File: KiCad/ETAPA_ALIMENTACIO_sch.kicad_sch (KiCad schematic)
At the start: 14 parts, among them U4 LM2596S-5, U6 LM1117DT-3.3

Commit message: V1 Routing
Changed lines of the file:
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@@
+	)
+	(junction
+		(at 170.18 85.09)
+		(diameter 0)
+		(color 0 0 0 0)
 	)
 	(junction
@@
 	)
 	(junction
-		(at 160.02 85.09)
-		(diameter 0)
-		(color 0 0 0 0)
-	)
-	(junction
 		(at 199.39 104.14)
 		(diameter 0)
@@
 	(wire
 		(pts
-			(xy 160.02 85.09) (xy 166.37 85.09)
+			(xy 138.43 85.09) (xy 166.37 85.09)
 		)
 		(stroke
@@
 		(pts
 			(xy 182.88 104.14) (xy 187.96 104.14)
-		)
-		(stroke
-			(width 0)
-			(type default)
-		)
-	)
-	(wire
-		(pts
-			(xy 138.43 85.09) (xy 160.02 85.09)
 		)
 		(stroke
@@
 		(dnp no)
 		(fields_autoplaced yes)
-		(property "Reference" "#FLG07"
+		(property "Reference" "#FLG04"
 			(at 63.5 86.995 0)
 			(effects
@@
 			(project "PROJECTE_EINES"
 				(path "/347831db-5db9-4aff-ad32-e56fd770e219/b8d025f8-884e-44af-b29b-4fb2140b95b4"
-					(reference "#FLG07")
+					(reference "#FLG04")
 					(unit 1)
 				)
@@
 		(dnp no)
 		(fields_autoplaced yes)
-		(property "Reference" "#PWR050"
+		(property "Reference" "#PWR031"
 			(at 60.96 88.9 0)
 			(effects
@@
 			(project "PROJECTE_EINES"
 				(path "/347831db-5db9-4aff-ad32-e56fd770e219/b8d025f8-884e-44af-b29b-4fb2140b95b4"
-					(reference "#PWR050")
+					(reference "#PWR031")
 					(unit 1)
 				)
@@
 	)
 	(symbol
+		(lib_id "power:+5V")
+		(at 170.18 85.09 0)
+		(unit 1)
+		(exclude_from_sim no)
+		(in_bom yes)
+		(on_board yes)
+		(dnp no)
+		(fields_autoplaced yes)
+		(property "Reference" "#PWR049"
+			(at 170.18 88.9 0)
+			(effects
+				(font
+					(size 1.27 1.27)
+				)
+				(hide yes)
+			)
+		)
+		(property "Value" "+5V"
+			(at 170.18 80.01 0)
+			(effects
+				(font
+					(size 1.27 1.27)
+				)
+			)
+		)
+		(property "Footprint" ""
+			(at 170.18 85.09 0)
+			(effects
+				(font
+					(size 1.27 1.27)
+				)
+				(hide yes)
+			)
+		)
+		(property "Datasheet" ""
+			(at 170.18 85.09 0)
+			(effects
+				(font
+					(size 1.27 1.27)
+				)
+				(hide yes)
+			)
+		)
+		(property "Description" "Power symbol creates a global label with name \"+5V\""
+			(at 170.18 85.09 0)
+			(effects
+				(font
+					(size 1.27 1.27)
+				)
+				(hide yes)
+			)
+		)
+		(pin "1"
+		)
+		(instances
+			(project ""
+				(path "/347831db-5db9-4aff-ad32-e56fd770e219/b8d025f8-884e-44af-b29b-4fb2140b95b4"
+					(reference "#PWR049")
+					(unit 1)
+				)
+			)
+		)
+	)
+	(symbol
 		(lib_id "Device:C")
 		(at 97.79 88.9 0)
@@
 		(dnp no)
 		(fields_autoplaced yes)
-		(property "Reference" "#PWR040"
+		(property "Reference" "#PWR041"
 			(at 182.88 111.76 0)
 			(effects
@@
 			(project "PROJECTE_EINES"
 				(path "/347831db-5db9-4aff-ad32-e56fd770e219/b8d025f8-884e-44af-b29b-4fb2140b95b4"
-					(reference "#PWR040")
+					(reference "#PWR041")
 					(unit 1)
 				)
@@
 					(unit 1)
 				)
-			)
-		)
-	)
-	(symbol
-		(lib_id "power:+5V")
-		(at 160.02 85.09 0)
-		(unit 1)
-		(exclude_from_sim no)
-		(in_bom yes)
-		(on_board yes)
-		(dnp no)
-		(fields_autoplaced yes)
-		(property "Reference" "#PWR037"
-			(at 160.02 88.9 0)
-			(effects
-				(font
-					(size 1.27 1.27)
-				)
-				(hide yes)
-			)
-		)
-		(property "Value" "+5V"
-			(at 160.02 80.01 0)
-			(effects
-				(font
-					(size 1.27 1.27)
-				)
-			)
-		)
-		(property "Footprint" ""
-			(at 160.02 85.09 0)
-			(effects
-				(font
-					(size 1.27 1.27)
-				)
-				(hide yes)
-			)
-		)
-		(property "Datasheet" ""
-			(at 160.02 85.09 0)
-			(effects
-				(font
-					(size 1.27 1.27)
-				)
-				(hide yes)
-			)
-		)
-		(property "Description" "Power symbol creates a global label with name \"+5V\""
-			(at 160.02 85.09 0)
-			(effects
-				(font
-					(size 1.27 1.27)
-				)
-				(hide yes)
-			)
-		)
-		(pin "1"
-		)
-		(instances
-			(project "PROJECTE_EINES"
-				(path "/347831db-5db9-4aff-ad32-e56fd770e219/b8d025f8-884e-44af-b29b-4fb2140b95b4"
-					(reference "#PWR037")
-					(unit 1)
-				)

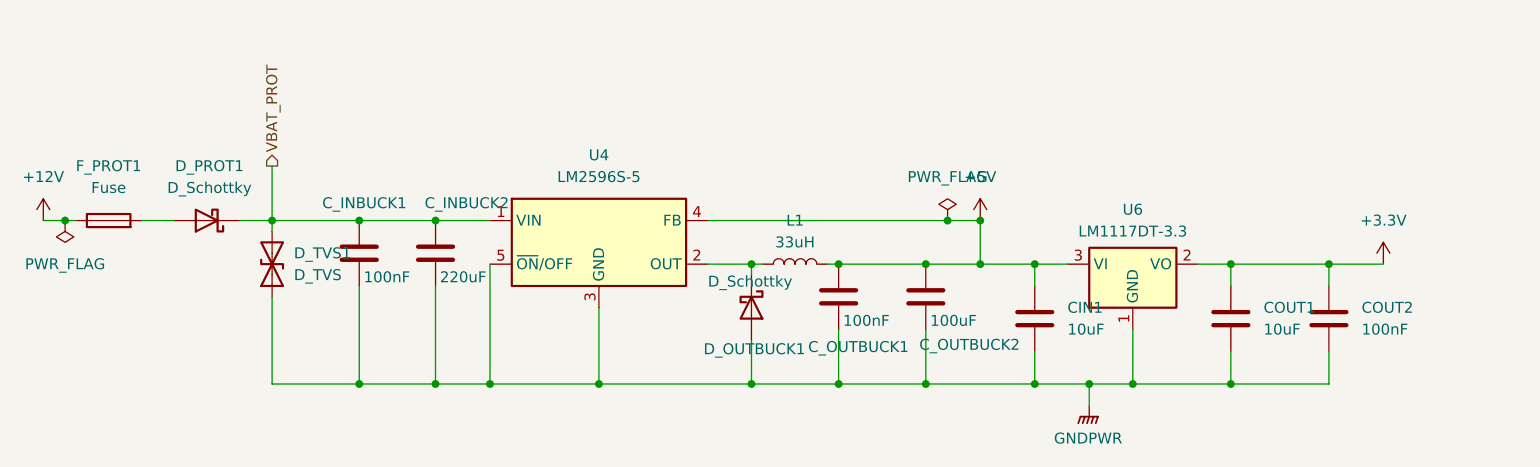
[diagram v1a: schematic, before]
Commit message: Actualització dels test points
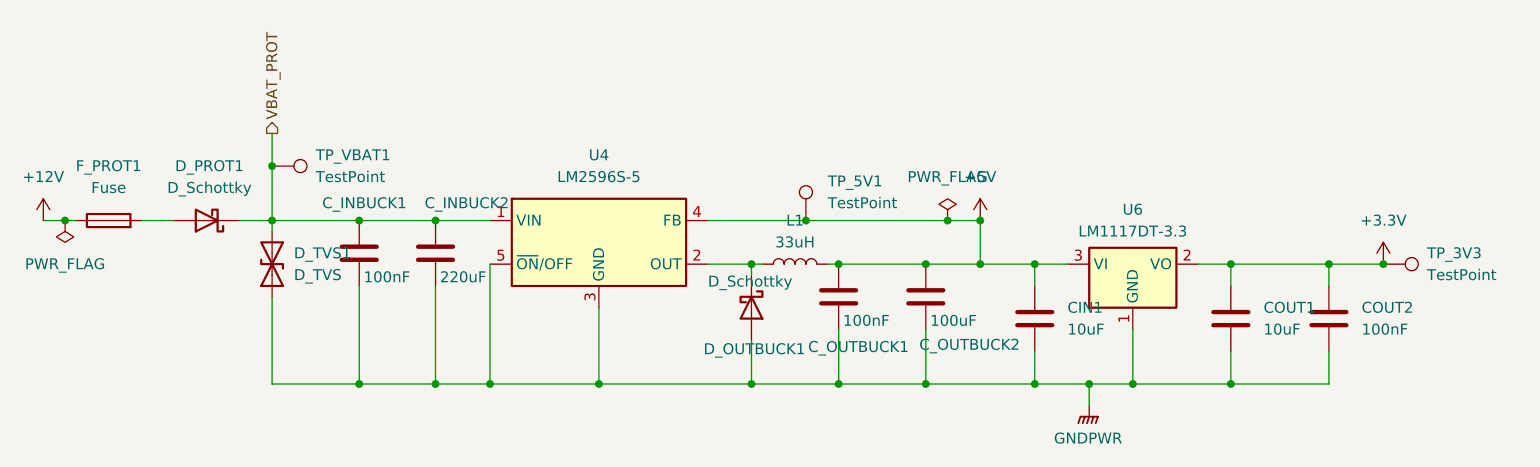
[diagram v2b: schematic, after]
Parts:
- added TP_3V3, TP_5V1, TP_VBAT1: TestPoint, TestPoint:TestPoint_Pad_D1.5mm, symbol Connector:TestPoint
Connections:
- net +3.3V: now also TP_3V3.1
- net +5V: now also TP_5V1.1
- net VBAT_PROT: now also TP_VBAT1.1
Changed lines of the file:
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@@
 	(paper "A4")
 	(junction
+		(at 217.17 90.17)
+		(diameter 0)
+		(color 0 0 0 0)
+	)
+	(junction
 		(at 97.79 85.09)
 		(diameter 0)
@@
 	)
 	(junction
+		(at 87.63 78.74)
+		(diameter 0)
+		(color 0 0 0 0)
+	)
+	(junction
 		(at 106.68 85.09)
 		(diameter 0)
@@
 	)
 	(junction
+		(at 149.86 85.09)
+		(diameter 0)
+		(color 0 0 0 0)
+	)
+	(junction
 		(at 166.37 85.09)
 		(diameter 0)
@@
 	(wire
 		(pts
+			(xy 149.86 85.09) (xy 166.37 85.09)
+		)
+		(stroke
+			(width 0)
+			(type default)
+		)
+	)
+	(wire
+		(pts
 			(xy 125.73 95.25) (xy 125.73 104.14)
 		)
@@
 	(wire
 		(pts
-			(xy 138.43 85.09) (xy 166.37 85.09)
+			(xy 138.43 85.09) (xy 149.86 85.09)
 		)
 		(stroke
@@
 	(wire
 		(pts
+			(xy 87.63 74.93) (xy 87.63 78.74)
+		)
+		(stroke
+			(width 0)
+			(type default)
+		)
+	)
+	(wire
+		(pts
+			(xy 106.68 85.09) (xy 113.03 85.09)
+		)
+		(stroke
+			(width 0)
+			(type default)
+		)
+	)
+	(wire
+		(pts
+			(xy 176.53 90.17) (xy 176.53 92.71)
+		)
+		(stroke
+			(width 0)
+			(type default)
+		)
+	)
+	(wire
+		(pts
+			(xy 87.63 85.09) (xy 97.79 85.09)
+		)
+		(stroke
+			(width 0)
+			(type default)
+		)
+	)
+	(wire
+		(pts
+			(xy 187.96 97.79) (xy 187.96 104.14)
+		)
+		(stroke
+			(width 0)
+			(type default)
+		)
+	)
+	(wire
+		(pts
+			(xy 106.68 92.71) (xy 106.68 104.14)
+		)
+		(stroke
+			(width 0)
+			(type default)
+		)
+	)
+	(wire
+		(pts
+			(xy 97.79 104.14) (xy 106.68 104.14)
+		)
+		(stroke
+			(width 0)
+			(type default)
+		)
+	)
+	(wire
+		(pts
+			(xy 199.39 100.33) (xy 199.39 104.14)
+		)
+		(stroke
+			(width 0)
+			(type default)
+		)
+	)
+	(wire
+		(pts
+			(xy 97.79 85.09) (xy 106.68 85.09)
+		)
+		(stroke
+			(width 0)
+			(type default)
+		)
+	)
+	(wire
+		(pts
+			(xy 182.88 104.14) (xy 187.96 104.14)
+		)
+		(stroke
+			(width 0)
+			(type default)
+		)
+	)
+	(wire
+		(pts
 			(xy 87.63 78.74) (xy 87.63 85.09)
-		)
-		(stroke
-			(width 0)
-			(type default)
-		)
-	)
-	(wire
-		(pts
-			(xy 106.68 85.09) (xy 113.03 85.09)
-		)
-		(stroke
-			(width 0)
-			(type default)
-		)
-	)
-	(wire
-		(pts
-			(xy 176.53 90.17) (xy 176.53 92.71)
-		)
-		(stroke
-			(width 0)
-			(type default)
-		)
-	)
-	(wire
-		(pts
-			(xy 87.63 85.09) (xy 97.79 85.09)
-		)
-		(stroke
-			(width 0)
-			(type default)
-		)
-	)
-	(wire
-		(pts
-			(xy 187.96 97.79) (xy 187.96 104.14)
-		)
-		(stroke
-			(width 0)
-			(type default)
-		)
-	)
-	(wire
-		(pts
-			(xy 106.68 92.71) (xy 106.68 104.14)
-		)
-		(stroke
-			(width 0)
-			(type default)
-		)
-	)
-	(wire
-		(pts
-			(xy 97.79 104.14) (xy 106.68 104.14)
-		)
-		(stroke
-			(width 0)
-			(type default)
-		)
-	)
-	(wire
-		(pts
-			(xy 199.39 100.33) (xy 199.39 104.14)
-		)
-		(stroke
-			(width 0)
-			(type default)
-		)
-	)
-	(wire
-		(pts
-			(xy 97.79 85.09) (xy 106.68 85.09)
-		)
-		(stroke
-			(width 0)
-			(type default)
-		)
-	)
-	(wire
-		(pts
-			(xy 182.88 104.14) (xy 187.96 104.14)
 		)
 		(stroke
@@
 	(hierarchical_label "VBAT_PROT"
 		(shape output)
-		(at 87.63 78.74 90)
+		(at 87.63 74.93 90)
 		(effects
 			(font
@@
 	)
 	(symbol
+		(lib_id "Connector:TestPoint")
+		(at 217.17 90.17 270)
+		(unit 1)
+		(exclude_from_sim no)
+		(in_bom yes)
+		(on_board yes)
+		(dnp no)
+		(fields_autoplaced yes)
+		(property "Reference" "TP_3V3"
+			(at 222.25 88.8999 90)
+			(effects
+				(font
+					(size 1.27 1.27)
+				)
+				(justify left)
+			)
+		)
+		(property "Value" "TestPoint"
+			(at 222.25 91.4399 90)
+			(effects
+				(font
+					(size 1.27 1.27)
+				)
+				(justify left)
+			)
+		)
+		(property "Footprint" "TestPoint:TestPoint_Pad_D1.5mm"
+			(at 217.17 95.25 0)
+			(effects
+				(font
+					(size 1.27 1.27)
+				)
+				(hide yes)
+			)
+		)
+		(property "Datasheet" "~"
+			(at 217.17 95.25 0)
+			(effects
+				(font
+					(size 1.27 1.27)
+				)
+				(hide yes)
+			)
+		)
+		(property "Description" "test point"
+			(at 217.17 90.17 0)
+			(effects
+				(font
+					(size 1.27 1.27)
+				)
+				(hide yes)
+			)
+		)
+		(pin "1"
+		)
+		(instances
+			(project "PROJECTE_EINES"
+				(path "/347831db-5db9-4aff-ad32-e56fd770e219/b8d025f8-884e-44af-b29b-4fb2140b95b4"
+					(reference "TP_3V3")
+					(unit 1)
+				)
+			)
+		)
+	)
+	(symbol
 		(lib_id "Device:C")
 		(at 106.68 88.9 0)
@@
 	)
 	(symbol
+		(lib_id "Connector:TestPoint")
+		(at 149.86 85.09 0)
+		(unit 1)
+		(exclude_from_sim no)
+		(in_bom yes)
+		(on_board yes)
+		(dnp no)
+		(fields_autoplaced yes)
+		(property "Reference" "TP_5V1"
+			(at 152.4 80.5179 0)
+			(effects
+				(font
+					(size 1.27 1.27)
+				)
+				(justify left)
+			)
+		)
+		(property "Value" "TestPoint"
+			(at 152.4 83.0579 0)
+			(effects
+				(font
+					(size 1.27 1.27)
+				)
+				(justify left)
+			)
+		)
+		(property "Footprint" "TestPoint:TestPoint_Pad_D1.5mm"
+			(at 154.94 85.09 0)
+			(effects
+				(font
+					(size 1.27 1.27)
+				)
+				(hide yes)
+			)
+		)
+		(property "Datasheet" "~"
+			(at 154.94 85.09 0)
+			(effects
+				(font
+					(size 1.27 1.27)
+				)
+				(hide yes)
+			)
+		)
+		(property "Description" "test point"
+			(at 149.86 85.09 0)
+			(effects
+				(font
+					(size 1.27 1.27)
+				)
+				(hide yes)
+			)
+		)
+		(pin "1"
+		)
+		(instances
+			(project "PROJECTE_EINES"
+				(path "/347831db-5db9-4aff-ad32-e56fd770e219/b8d025f8-884e-44af-b29b-4fb2140b95b4"
+					(reference "TP_5V1")
+					(unit 1)
+				)
+			)
+		)
+	)
+	(symbol
 		(lib_id "Device:D_TVS")
 		(at 87.63 90.17 90)
@@
 					(unit 1)
 				)
+			)
+		)
+	)
+	(symbol
+		(lib_id "Connector:TestPoint")
+		(at 87.63 78.74 270)
+		(unit 1)
+		(exclude_from_sim no)
+		(in_bom yes)
+		(on_board yes)
+		(dnp no)
+		(fields_autoplaced yes)
+		(property "Reference" "TP_VBAT1"
+			(at 92.71 77.4699 90)
+			(effects
+				(font
+					(size 1.27 1.27)
+				)
+				(justify left)
+			)
+		)
+		(property "Value" "TestPoint"
+			(at 92.71 80.0099 90)
+			(effects
+				(font
+					(size 1.27 1.27)
+				)
+				(justify left)
+			)
+		)
+		(property "Footprint" "TestPoint:TestPoint_Pad_D1.5mm"
+			(at 87.63 83.82 0)
+			(effects
+				(font
+					(size 1.27 1.27)
+				)
+				(hide yes)
+			)
+		)
+		(property "Datasheet" "~"
+			(at 87.63 83.82 0)
+			(effects
+				(font
+					(size 1.27 1.27)
+				)
+				(hide yes)
+			)
+		)
+		(property "Description" "test point"
+			(at 87.63 78.74 0)
+			(effects
+				(font
+					(size 1.27 1.27)
+				)
+				(hide yes)
+			)
+		)
+		(pin "1"
+		)
+		(instances
+			(project ""
+				(path "/347831db-5db9-4aff-ad32-e56fd770e219/b8d025f8-884e-44af-b29b-4fb2140b95b4"
+					(reference "TP_VBAT1")
+					(unit 1)
+				)

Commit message: Versio final KiCad, BOM i Diagrama de Blocs
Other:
- note added: "Disminueix el voltatge de 12V a 5V"
- note added: "Redueix el voltatge de 5V a 3.3V"
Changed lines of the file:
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@@
 	(generator_version "9.0")
 	(paper "A4")
+	(text "Disminueix el voltatge de 12V a 5V"
+		(exclude_from_sim no)
+		(at 113.538 72.39 0)
+		(effects
+			(font
+				(size 1.27 1.27)
+			)
+		)
+	)
+	(text "Redueix el voltatge de 5V a 3.3V"
+		(exclude_from_sim no)
+		(at 192.024 78.74 0)
+		(effects
+			(font
+				(size 1.27 1.27)
+			)
+		)
+	)
 	(junction
 		(at 217.17 90.17)

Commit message: Versio final
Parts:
- CIN1, COUT1: footprint Capacitor_SMD:C_1206_3216Metric -> Capacitor_SMD:C_0805_2012Metric
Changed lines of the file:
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@@
 			)
 		)
-		(property "Footprint" "Capacitor_SMD:C_1206_3216Metric"
+		(property "Footprint" "Capacitor_SMD:C_0805_2012Metric"
 			(at 200.3552 100.33 0)
 			(effects
@@
 			)
 		)
-		(property "Footprint" "Capacitor_SMD:C_1206_3216Metric"
+		(property "Footprint" "Capacitor_SMD:C_0805_2012Metric"
 			(at 177.4952 100.33 0)
 			(effects

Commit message: Versió Final projecte
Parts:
- C17: renamed from CIN1; footprint Capacitor_SMD:C_0805_2012Metric -> Capacitor_SMD:C_1206_3216Metric
- C19: renamed from COUT1; footprint Capacitor_SMD:C_0805_2012Metric -> Capacitor_SMD:C_1206_3216Metric
- renumbered C_INBUCK1 to C11, C_INBUCK2 to C12, C_OUTBUCK1 to C13, C_OUTBUCK2 to C16, COUT2 to C20, D_PROT1 to D1, D_TVS1 to D2, D_OUTBUCK1 to D3, F_PROT1 to F1, TP_3V3 to TP_3V1
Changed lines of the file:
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@@
 		(dnp no)
 		(fields_autoplaced yes)
-		(property "Reference" "COUT1"
+		(property "Reference" "C19"
 			(at 203.2 95.2499 0)
 			(effects
@@
 			)
 		)
-		(property "Footprint" "Capacitor_SMD:C_0805_2012Metric"
+		(property "Footprint" "Capacitor_SMD:C_1206_3216Metric"
 			(at 200.3552 100.33 0)
 			(effects
@@
 			(project "PROJECTE_EINES"
 				(path "/347831db-5db9-4aff-ad32-e56fd770e219/b8d025f8-884e-44af-b29b-4fb2140b95b4"
-					(reference "COUT1")
+					(reference "C19")
 					(unit 1)
 				)
@@
 		(dnp no)
 		(fields_autoplaced yes)
-		(property "Reference" "TP_3V3"
+		(property "Reference" "TP_3V1"
 			(at 222.25 88.8999 90)
 			(effects
@@
 			(project "PROJECTE_EINES"
 				(path "/347831db-5db9-4aff-ad32-e56fd770e219/b8d025f8-884e-44af-b29b-4fb2140b95b4"
-					(reference "TP_3V3")
+					(reference "TP_3V1")
 					(unit 1)
 				)
@@
 		(on_board yes)
 		(dnp no)
-		(property "Reference" "C_INBUCK2"
+		(property "Reference" "C12"
 			(at 105.41 83.058 0)
 			(effects
@@
 			(project "PROJECTE_EINES"
 				(path "/347831db-5db9-4aff-ad32-e56fd770e219/b8d025f8-884e-44af-b29b-4fb2140b95b4"
-					(reference "C_INBUCK2")
+					(reference "C12")
 					(unit 1)
 				)
@@
 		(dnp no)
 		(fields_autoplaced yes)
-		(property "Reference" "F_PROT1"
+		(property "Reference" "F1"
 			(at 68.58 78.74 90)
 			(effects
@@
 			(project "PROJECTE_EINES"
 				(path "/347831db-5db9-4aff-ad32-e56fd770e219/b8d025f8-884e-44af-b29b-4fb2140b95b4"
-					(reference "F_PROT1")
+					(reference "F1")
 					(unit 1)
 				)
@@
 		(dnp no)
 		(fields_autoplaced yes)
-		(property "Reference" "CIN1"
+		(property "Reference" "C17"
 			(at 180.34 95.2499 0)
 			(effects
@@
 			)
 		)
-		(property "Footprint" "Capacitor_SMD:C_0805_2012Metric"
+		(property "Footprint" "Capacitor_SMD:C_1206_3216Metric"
 			(at 177.4952 100.33 0)
 			(effects
@@
 			(project "PROJECTE_EINES"
 				(path "/347831db-5db9-4aff-ad32-e56fd770e219/b8d025f8-884e-44af-b29b-4fb2140b95b4"
-					(reference "CIN1")
+					(reference "C17")
 					(unit 1)
 				)
@@
 		(on_board yes)
 		(dnp no)
-		(property "Reference" "C_OUTBUCK2"
+		(property "Reference" "C16"
 			(at 163.068 99.568 0)
 			(effects
@@
 			(project "PROJECTE_EINES"
 				(path "/347831db-5db9-4aff-ad32-e56fd770e219/b8d025f8-884e-44af-b29b-4fb2140b95b4"
-					(reference "C_OUTBUCK2")
+					(reference "C16")
 					(unit 1)
 				)
@@
 		(dnp no)
 		(fields_autoplaced yes)
-		(property "Reference" "D_PROT1"
+		(property "Reference" "D1"
 			(at 80.3275 78.74 0)
 			(effects
@@
 			(project "PROJECTE_EINES"
 				(path "/347831db-5db9-4aff-ad32-e56fd770e219/b8d025f8-884e-44af-b29b-4fb2140b95b4"
-					(reference "D_PROT1")
+					(reference "D1")
 					(unit 1)
 				)
@@
 		(dnp no)
 		(fields_autoplaced yes)
-		(property "Reference" "#FLG04"
+		(property "Reference" "#FLG05"
 			(at 63.5 86.995 0)
 			(effects
@@
 			(project "PROJECTE_EINES"
 				(path "/347831db-5db9-4aff-ad32-e56fd770e219/b8d025f8-884e-44af-b29b-4fb2140b95b4"
-					(reference "#FLG04")
+					(reference "#FLG05")
 					(unit 1)
 				)
@@
 		(dnp no)
 		(fields_autoplaced yes)
-		(property "Reference" "#PWR049"
+		(property "Reference" "#PWR038"
 			(at 170.18 88.9 0)
 			(effects
@@
 			(project ""
 				(path "/347831db-5db9-4aff-ad32-e56fd770e219/b8d025f8-884e-44af-b29b-4fb2140b95b4"
-					(reference "#PWR049")
+					(reference "#PWR038")
 					(unit 1)
 				)
@@
 		(on_board yes)
 		(dnp no)
-		(property "Reference" "C_INBUCK1"
+		(property "Reference" "C11"
 			(at 93.472 83.058 0)
 			(effects
@@
 			(project "PROJECTE_EINES"
 				(path "/347831db-5db9-4aff-ad32-e56fd770e219/b8d025f8-884e-44af-b29b-4fb2140b95b4"
-					(reference "C_INBUCK1")
+					(reference "C11")
 					(unit 1)
 				)
@@
 		(dnp no)
 		(fields_autoplaced yes)
-		(property "Reference" "COUT2"
+		(property "Reference" "C20"
 			(at 214.63 95.2499 0)
 			(effects
@@
 			(project "PROJECTE_EINES"
 				(path "/347831db-5db9-4aff-ad32-e56fd770e219/b8d025f8-884e-44af-b29b-4fb2140b95b4"
-					(reference "COUT2")
+					(reference "C20")
 					(unit 1)
 				)
@@
 		(dnp no)
 		(fields_autoplaced yes)
-		(property "Reference" "#FLG05"
+		(property "Reference" "#FLG06"
 			(at 166.37 83.185 0)
 			(effects
@@
 			(project "PROJECTE_EINES"
 				(path "/347831db-5db9-4aff-ad32-e56fd770e219/b8d025f8-884e-44af-b29b-4fb2140b95b4"
-					(reference "#FLG05")
+					(reference "#FLG06")
 					(unit 1)
 				)
@@
 		(dnp no)
 		(fields_autoplaced yes)
-		(property "Reference" "D_TVS1"
+		(property "Reference" "D2"
 			(at 90.17 88.8999 90)
 			(effects
@@
 			(project "PROJECTE_EINES"
 				(path "/347831db-5db9-4aff-ad32-e56fd770e219/b8d025f8-884e-44af-b29b-4fb2140b95b4"
-					(reference "D_TVS1")
+					(reference "D2")
 					(unit 1)
 				)
@@
 		(on_board yes)
 		(dnp no)
-		(property "Reference" "C_OUTBUCK1"
+		(property "Reference" "C13"
 			(at 150.114 99.822 0)
 			(effects
@@
 			(project "PROJECTE_EINES"
 				(path "/347831db-5db9-4aff-ad32-e56fd770e219/b8d025f8-884e-44af-b29b-4fb2140b95b4"
-					(reference "C_OUTBUCK1")
+					(reference "C13")
 					(unit 1)
 				)
@@
 		(dnp no)
 		(fields_autoplaced yes)
-		(property "Reference" "#PWR041"
+		(property "Reference" "#PWR040"
 			(at 182.88 111.76 0)
 			(effects
@@
 			(project "PROJECTE_EINES"
 				(path "/347831db-5db9-4aff-ad32-e56fd770e219/b8d025f8-884e-44af-b29b-4fb2140b95b4"
-					(reference "#PWR041")
+					(reference "#PWR040")
 					(unit 1)
 				)
@@
 		(on_board yes)
 		(dnp no)
-		(property "Reference" "D_OUTBUCK1"
+		(property "Reference" "D3"
 			(at 137.922 100.076 90)
 			(effects
@@
 			(project "PROJECTE_EINES"
 				(path "/347831db-5db9-4aff-ad32-e56fd770e219/b8d025f8-884e-44af-b29b-4fb2140b95b4"
-					(reference "D_OUTBUCK1")
-					(unit 1)
-				)
+					(reference "D3")
+					(unit 1)
+				)
